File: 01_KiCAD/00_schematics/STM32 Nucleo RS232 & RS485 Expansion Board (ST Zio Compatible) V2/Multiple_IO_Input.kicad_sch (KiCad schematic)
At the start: 10 parts, among them J6 SW_ENA, U4 SN74LVC245ADBR

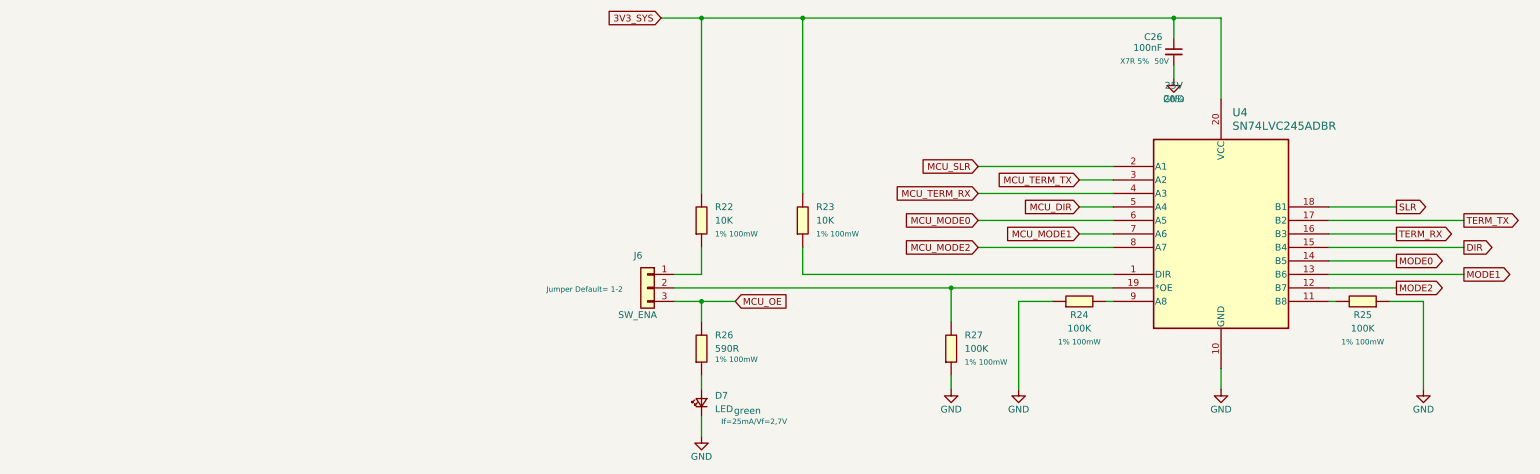
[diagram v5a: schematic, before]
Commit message: Complete redesign
Redesigned the complete board. Added hardware termination jumpers for 1120R resistors for RS485. Changes footprint, package size and simplified values between capacitors.
Still need to re-route the entire board :-(
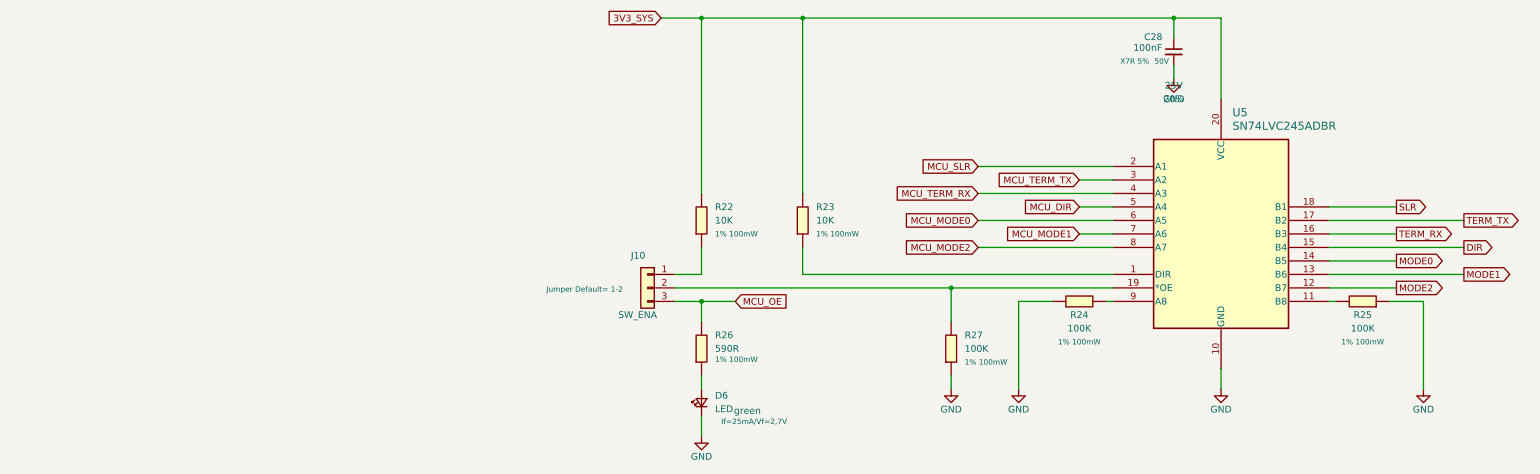
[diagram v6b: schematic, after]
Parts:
- renumbered C26 to C28, D7 to D6, J6 to J10, U4 to U5

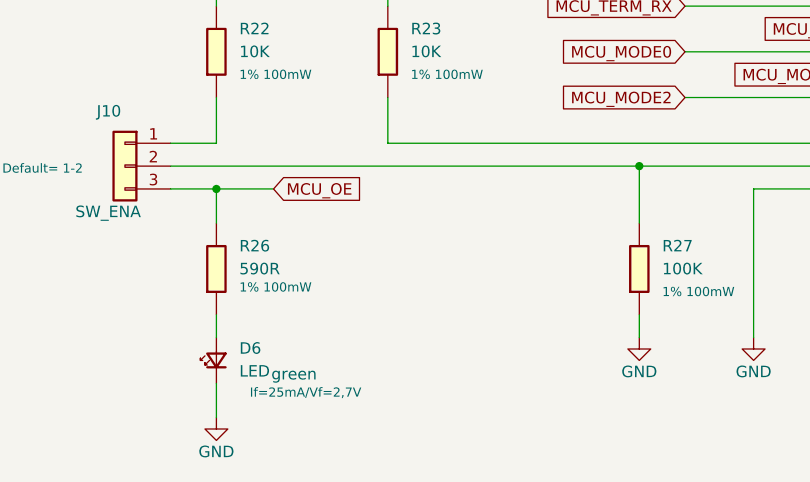
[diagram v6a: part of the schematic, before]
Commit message: Small changes to schematics & PCB work
Made some minor adjustments to the schematics, updated the PCB accordingly.
Placed all the components on the board and did some of the routing.
Updated the 3D models of all the components.
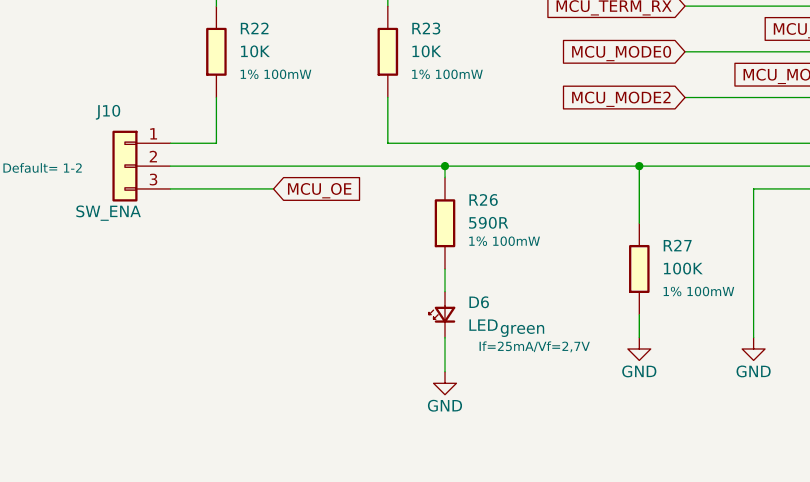
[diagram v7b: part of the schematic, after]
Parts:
- C28: footprint PCM_SparkFun-Capacitor:C_0603_1608Metric -> Capacitor_SMD:C_0805_2012Metric
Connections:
- net MCU_OE: no longer R26.1
- net at J10.2 (Pin_2), R27.1, U5.19 (*OE): now also R26.1
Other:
- moved on the sheet: D6, R26
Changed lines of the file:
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@@
 	)
 	(junction
-		(at 85.09 99.06)
+		(at 110.49 96.52)
 		(diameter 0)
 		(color 0 0 0 0)
@@
 	(wire
 		(pts
-			(xy 80.01 96.52) (xy 132.08 96.52)
-		)
-		(stroke
-			(width 0)
-			(type default)
-		)
-	)
-	(wire
-		(pts
-			(xy 85.09 99.06) (xy 91.44 99.06)
+			(xy 80.01 96.52) (xy 110.49 96.52)
+		)
+		(stroke
+			(width 0)
+			(type default)
+		)
+	)
+	(wire
+		(pts
+			(xy 80.01 99.06) (xy 91.44 99.06)
 		)
 		(stroke
@@
 	(wire
 		(pts
-			(xy 80.01 99.06) (xy 85.09 99.06)
-		)
-		(stroke
-			(width 0)
-			(type default)
-		)
-	)
-	(wire
-		(pts
 			(xy 151.13 99.06) (xy 144.78 99.06)
 		)
@@
 	(wire
 		(pts
-			(xy 85.09 113.03) (xy 85.09 115.57)
+			(xy 110.49 107.95) (xy 110.49 110.49)
 		)
 		(stroke
@@
 	(wire
 		(pts
-			(xy 85.09 120.65) (xy 85.09 124.46)
+			(xy 110.49 115.57) (xy 110.49 119.38)
 		)
 		(stroke
@@
 	(wire
 		(pts
-			(xy 85.09 102.87) (xy 85.09 99.06)
-		)
-		(stroke
-			(width 0)
-			(type default)
-		)
-	)
-	(wire
-		(pts
 			(xy 144.78 99.06) (xy 144.78 115.57)
 		)
@@
 	(wire
 		(pts
+			(xy 110.49 96.52) (xy 132.08 96.52)
+		)
+		(stroke
+			(width 0)
+			(type default)
+		)
+	)
+	(wire
+		(pts
 			(xy 104.14 93.98) (xy 162.56 93.98)
+		)
+		(stroke
+			(width 0)
+			(type default)
+		)
+	)
+	(wire
+		(pts
+			(xy 110.49 96.52) (xy 110.49 97.79)
 		)
 		(stroke
@@
 	(symbol
 		(lib_id "PCM_SparkFun-PowerSymbol:GND")
-		(at 85.09 124.46 0)
+		(at 110.49 119.38 0)
 		(mirror y)
 		(unit 1)
@@
 		(fields_autoplaced yes)
 		(property "Reference" "#PWR046"
-			(at 85.09 130.81 0)
+			(at 110.49 125.73 0)
 			(effects
 				(font
@@
 		)
 		(property "Value" "GND"
-			(at 85.09 128.27 0)
+			(at 110.49 123.19 0)
 			(do_not_autoplace yes)
 			(effects
@@
 		)
 		(property "Footprint" ""
-			(at 85.09 124.46 0)
+			(at 110.49 119.38 0)
 			(effects
 				(font
@@
 		)
 		(property "Datasheet" ""
-			(at 85.09 124.46 0)
+			(at 110.49 119.38 0)
 			(effects
 				(font
@@
 		)
 		(property "Description" "Power symbol creates a global label with name \"GND\" , ground"
-			(at 85.09 133.35 0)
+			(at 110.49 128.27 0)
 			(effects
 				(font
@@
 			)
 		)
-		(property "Footprint" "PCM_SparkFun-Capacitor:C_0603_1608Metric"
+		(property "Footprint" "Capacitor_SMD:C_0805_2012Metric"
 			(at 173.99 63.5 0)
 			(effects
@@
 	(symbol
 		(lib_id "PCM_fab:R_0603")
-		(at 85.09 107.95 0)
+		(at 110.49 102.87 0)
 		(unit 1)
 		(exclude_from_sim no)
@@
 		(dnp no)
 		(property "Reference" "R26"
-			(at 87.63 105.4099 0)
+			(at 113.03 100.3299 0)
 			(effects
 				(font
@@
 		)
 		(property "Value" "590R"
-			(at 87.63 107.9499 0)
+			(at 113.03 102.8699 0)
 			(effects
 				(font
@@
 		)
 		(property "Footprint" "PCM_fab:R_0603"
-			(at 85.09 107.95 90)
+			(at 110.49 102.87 90)
 			(effects
 				(font
@@
 		)
 		(property "Datasheet" "~"
-			(at 85.09 107.95 0)
+			(at 110.49 102.87 0)
 			(effects
 				(font
@@
 		)
 		(property "Description" "Resistor"
-			(at 85.09 107.95 0)
+			(at 110.49 102.87 0)
 			(effects
 				(font
@@
 		)
 		(property "Manufacturer" "YAGEO"
-			(at 85.09 107.95 0)
+			(at 110.49 102.87 0)
 			(effects
 				(font
@@
 		)
 		(property "MPN" "RC0603FR-071KL"
-			(at 85.09 107.95 0)
+			(at 110.49 102.87 0)
 			(effects
 				(font
@@
 		)
 		(property "Supplier" ""
-			(at 85.09 107.95 0)
+			(at 110.49 102.87 0)
 			(effects
 				(font
@@
 		)
 		(property "SPN" ""
-			(at 85.09 107.95 0)
+			(at 110.49 102.87 0)
 			(effects
 				(font
@@
 		)
 		(property "LCSC" "C22548"
-			(at 85.09 107.95 0)
+			(at 110.49 102.87 0)
 			(effects
 				(font
@@
 		)
 		(property "Package" "0603"
-			(at 85.09 107.95 0)
+			(at 110.49 102.87 0)
 			(effects
 				(font
@@
 		)
 		(property "Type" "SMD"
-			(at 85.09 107.95 0)
+			(at 110.49 102.87 0)
 			(effects
 				(font
@@
 		)
 		(property "DNP" ""
-			(at 85.09 107.95 0)
+			(at 110.49 102.87 0)
 			(effects
 				(font
@@
 		)
 		(property "Dielectric" ""
-			(at 85.09 107.95 0)
+			(at 110.49 102.87 0)
 			(effects
 				(font
@@
 		)
 		(property "Voltage Rating" "1% 100mW"
-			(at 87.63 109.982 0)
+			(at 113.03 104.902 0)
 			(effects
 				(font
@@
 		)
 		(property "DESCRIPTION" ""
-			(at 85.09 107.95 0)
+			(at 110.49 102.87 0)
 			(effects
 				(font
@@
 		)
 		(property "HEIGHT" ""
-			(at 85.09 107.95 0)
+			(at 110.49 102.87 0)
 			(effects
 				(font
@@
 		)
 		(property "MANUFACTURER_NAME" ""
-			(at 85.09 107.95 0)
+			(at 110.49 102.87 0)
 			(effects
 				(font
@@
 		)
 		(property "MANUFACTURER_PART_NUMBER" ""
-			(at 85.09 107.95 0)
+			(at 110.49 102.87 0)
 			(effects
 				(font
@@
 		)
 		(property "MOUSER_PART_NUMBER" ""
-			(at 85.09 107.95 0)
+			(at 110.49 102.87 0)
 			(effects
 				(font
@@
 	(symbol
 		(lib_id "PCM_SparkFun-LED:LED")
-		(at 85.09 118.11 90)
+		(at 110.49 113.03 90)
 		(unit 1)
 		(exclude_from_sim no)
@@
 		(dnp no)
 		(property "Reference" "D6"
-			(at 87.63 116.7764 90)
+			(at 113.03 111.6964 90)
 			(effects
 				(font
@@
 		)
 		(property "Value" "LED"
-			(at 87.63 119.3164 90)
+			(at 113.03 114.2364 90)
 			(effects
 				(font
@@
 		)
 		(property "Footprint" "IN-S63AT:LED_0603_WRE"
-			(at 90.17 118.11 0)
+			(at 115.57 113.03 0)
 			(effects
 				(font
@@
 		)
 		(property "Datasheet" "~"
-			(at 92.71 118.11 0)
+			(at 118.11 113.03 0)
 			(effects
 				(font
@@
 		)
 		(property "Description" "Light emitting diode"
-			(at 97.79 118.11 0)
+			(at 123.19 113.03 0)
 			(effects
 				(font
@@
 		)
 		(property "PROD_ID" "LED-"
-			(at 95.25 118.11 0)
+			(at 120.65 113.03 0)
 			(effects
 				(font
@@
 		)
 		(property "Manufacturer" "Inolux"
-			(at 85.09 118.11 0)
+			(at 110.49 113.03 0)
 			(effects
 				(font
@@
 		)
 		(property "MPN" "IN-S63AT5G"
-			(at 85.09 118.11 0)
+			(at 110.49 113.03 0)
 			(effects
 				(font
@@
 		)
 		(property "Supplier" ""
-			(at 85.09 118.11 0)
+			(at 110.49 113.03 0)
 			(effects
 				(font
@@
 		)
 		(property "SPN" ""
-			(at 85.09 118.11 0)
+			(at 110.49 113.03 0)
 			(effects
 				(font
@@
 		)
 		(property "LCSC" "C5656662"
-			(at 85.09 118.11 0)
+			(at 110.49 113.03 0)
 			(effects
 				(font
@@
 		)
 		(property "Package" "0603"
-			(at 85.09 118.11 0)
+			(at 110.49 113.03 0)
 			(effects
 				(font
@@
 		)
 		(property "Type" "SMD"
-			(at 85.09 118.11 0)
+			(at 110.49 113.03 0)
 			(effects
 				(font
@@
 		)
 		(property "DNP" ""
-			(at 85.09 118.11 0)
+			(at 110.49 113.03 0)
 			(effects
 				(font
@@
 		)
 		(property "Dielectric" ""
-			(at 85.09 118.11 0)
+			(at 110.49 113.03 0)
 			(effects
 				(font
@@
 		)
 		(property "Voltage Rating" "If=25mA/Vf=2,7V "
-			(at 94.996 121.666 90)
+			(at 120.396 116.586 90)
 			(effects
 				(font
@@
 		)
 		(property "Color" "green"
-			(at 93.726 119.634 90)
+			(at 119.126 114.554 90)
 			(effects
 				(font
@@
 		)
 		(property "DESCRIPTION" ""
-			(at 85.09 118.11 90)
+			(at 110.49 113.03 90)
 			(effects
 				(font
@@
 		)
 		(property "HEIGHT" ""
-			(at 85.09 118.11 90)
+			(at 110.49 113.03 90)
 			(effects
 				(font
@@
 		)
 		(property "MANUFACTURER_NAME" ""
-			(at 85.09 118.11 90)
+			(at 110.49 113.03 90)
 			(effects
 				(font
@@
 		)
 		(property "MANUFACTURER_PART_NUMBER" ""
-			(at 85.09 118.11 90)
+			(at 110.49 113.03 90)
 			(effects
 				(font
@@
 		)
 		(property "MOUSER_PART_NUMBER" ""
-			(at 85.09 118.11 90)
-			(effects
-				(font
+			(at 110.49 113.03 90)
+			(effects
+				(font

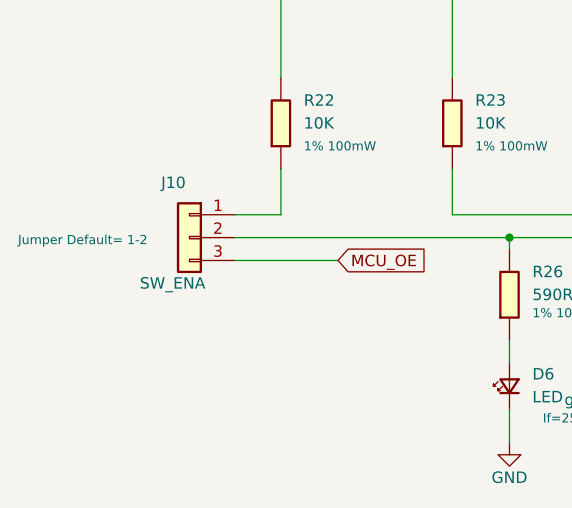
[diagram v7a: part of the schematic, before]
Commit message: Finalizing board layout & routing
Set HW Revision of board to: HW REV A0.1 and placed this as copper text on the back of the PCB.
Run DRC to see any critical errors. Resolved some minor silkscreen issues with overlapping text.
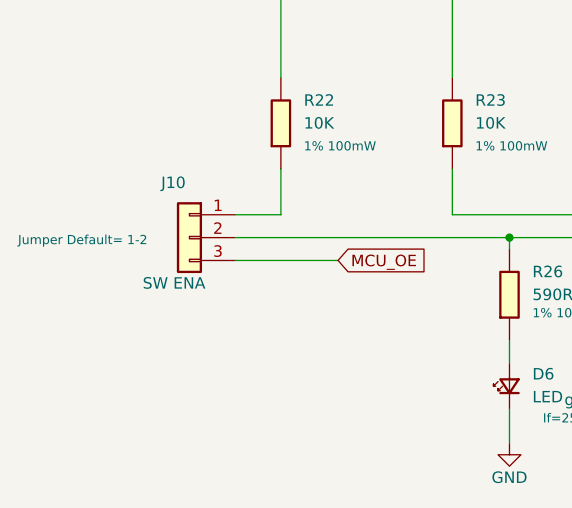
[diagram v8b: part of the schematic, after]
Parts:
- J10: value SW_ENA -> SW ENA
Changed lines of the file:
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@@
 			)
 		)
-		(property "Value" "SW_ENA"
+		(property "Value" "SW ENA"
 			(at 76.708 101.6 0)
 			(effects
